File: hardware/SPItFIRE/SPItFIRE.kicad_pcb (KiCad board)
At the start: 2 copper layers, 182.9 x 151.8 mm, 36 parts, among them J1 Compact Host, J10 ISP, J11 Joystick A, J12 Joystick B, J13 Peripheral DE-9, J14 Peripheral User Port, J2 User Port Host, J3 User Port Passthrough, J4 SD Card Adapter, J5 DeadOnRTC, J6 SPI_4, J7 SPI_5, J8 SPI_6, J9 SPI_7, U1 74HC138, U2 ATmega1284P-A, Y1 Crystal

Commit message: Work in progress on layout and routing
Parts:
- moved J1 0.20 mm to (59.4, 66.2)
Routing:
- net ~{SS_5}: track 0.00 -> 111.7 mm, vias 0 -> 2
- net PD1: track 109.8 -> 10.3 mm, vias 3 -> 1
- net ~{SS_3}: track 0.00 -> 85.3 mm, vias 0 -> 2
- net GND: track 128.6 -> 212.5 mm
- net AVCC: track 98.7 -> 24.8 mm, vias 2 -> 0
- net ~{SS_4}: track 20.3 -> 89.2 mm, vias 1 -> 2
- net PA3: track 81.0 -> 16.7 mm, vias 4 -> 2
- net PA1: track 83.4 -> 19.3 mm, vias 4 -> 2
- net PD5: track 62.4 -> 3.43 mm, vias 2 -> 1
- net PB1: track 80.4 -> 22.8 mm, vias 4 -> 2
- net PB3: track 81.5 -> 25.8 mm, vias 4 -> 2
- net PD0: track 99.5 -> 44.4 mm, vias 2 -> 1
- net PC7: track 63.7 -> 11.0 mm, vias 4 -> 2
- net ~{SS_1}: track 3.88 -> 55.4 mm, vias 0 -> 4
- net PA7: track 60.6 -> 10.1 mm, vias 4 -> 2
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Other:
- board size 182.9 x 151.8 mm -> 153 x 151.8 mm

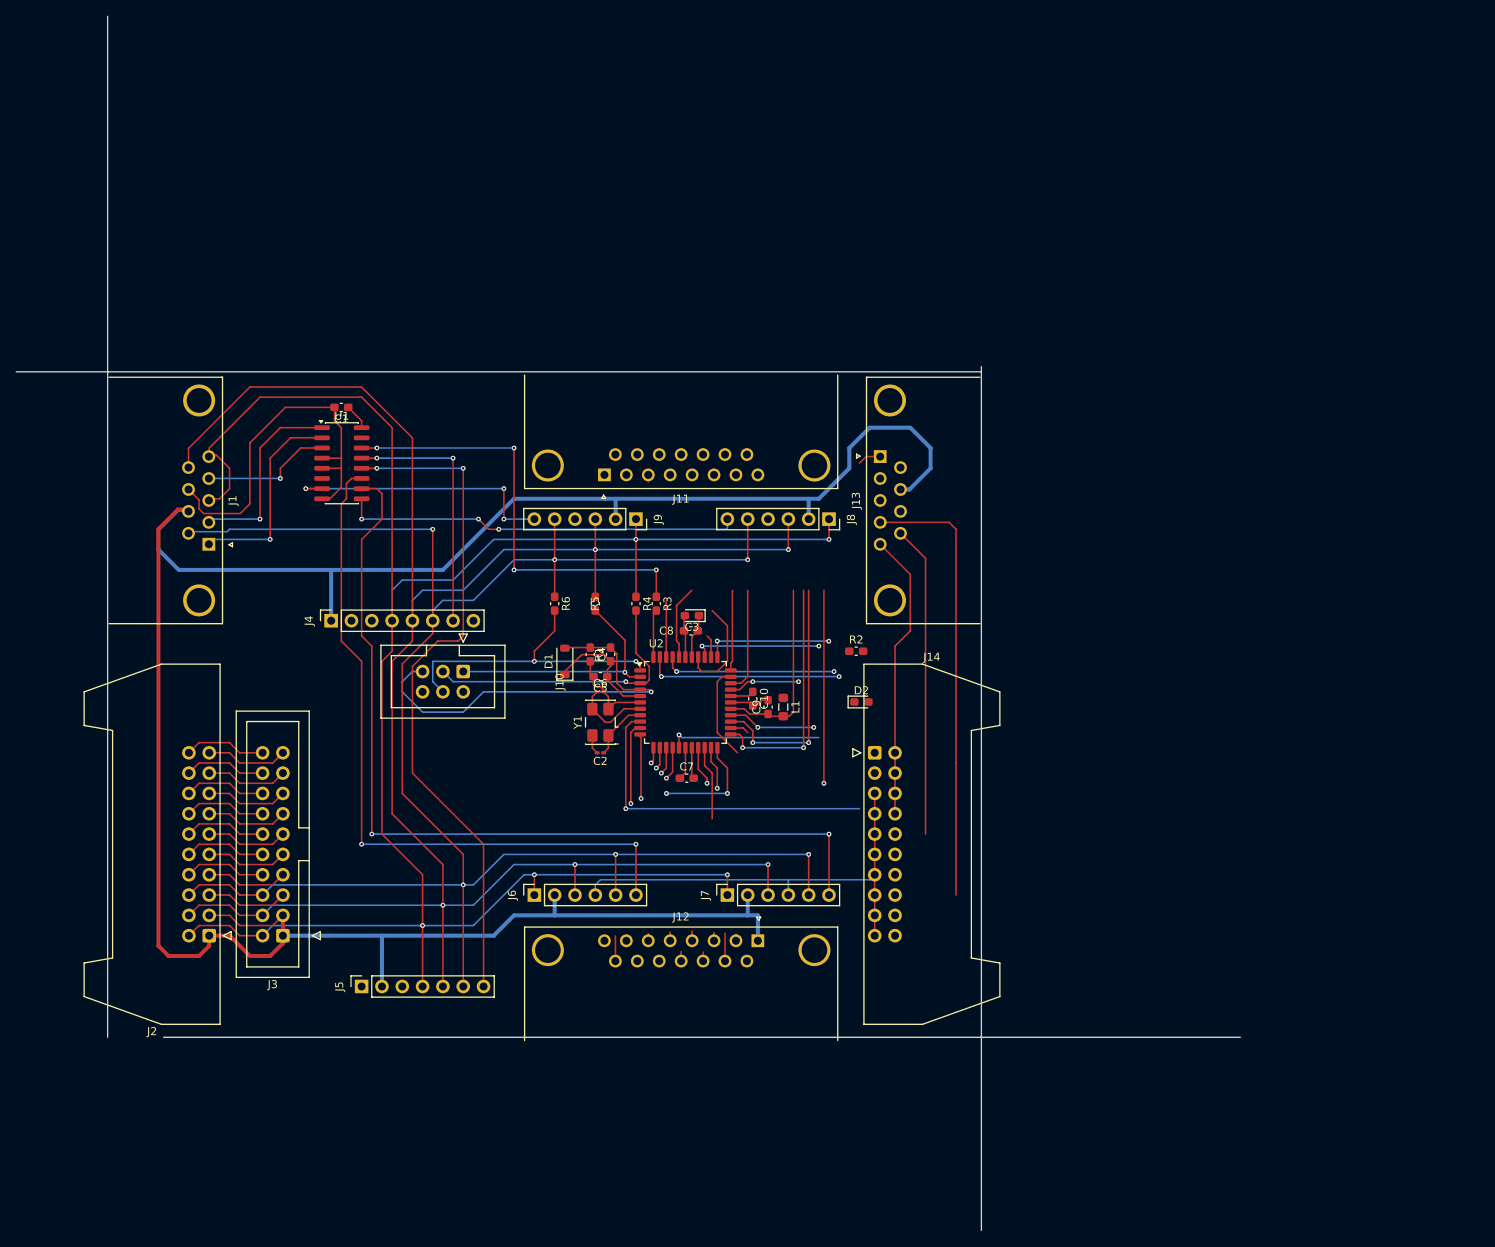
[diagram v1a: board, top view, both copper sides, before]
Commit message: Completed layout and routing. Now need to work through the few DRC errors
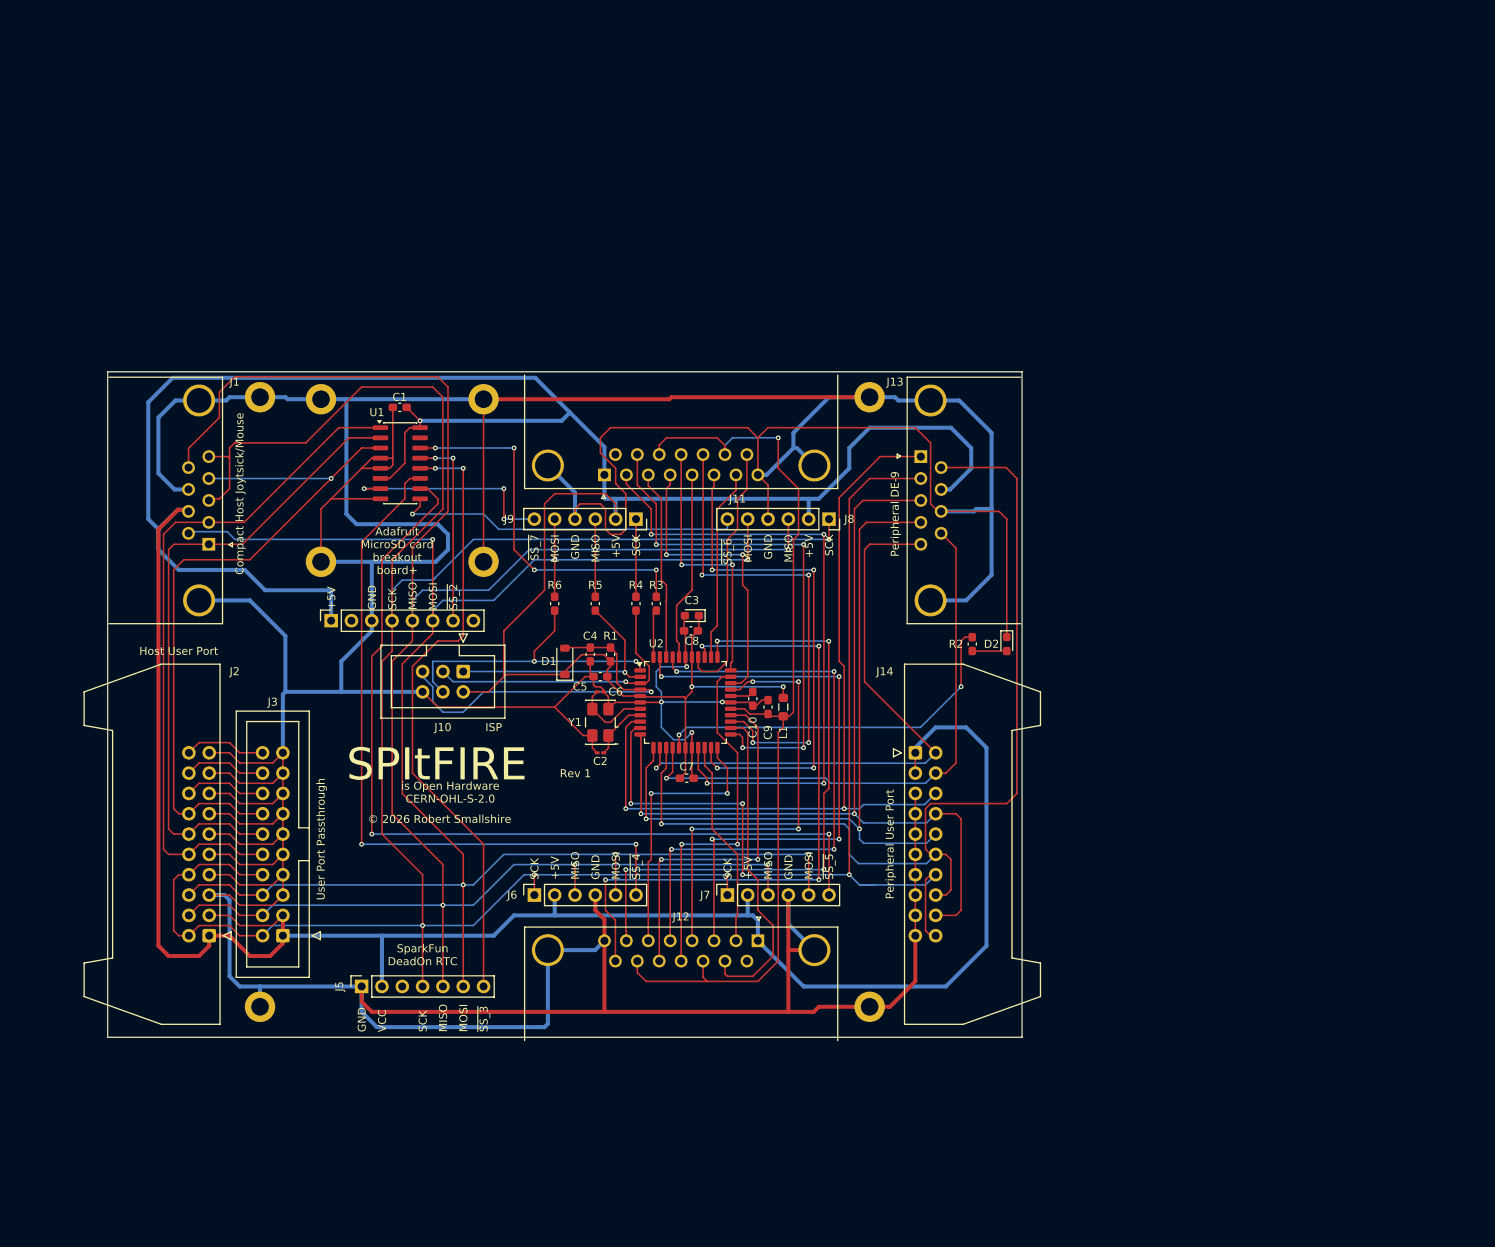
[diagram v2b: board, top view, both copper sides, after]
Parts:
- added H301: MountingHole_Pad, MountingHole:MountingHole_2.2mm_M2_DIN965_Pad, F.Cu at (78.7, 129.5)
- added H302: MountingHole_Pad, MountingHole:MountingHole_2.2mm_M2_DIN965_Pad, F.Cu at (154.9, 129.5)
- added H303: MountingHole_Pad, MountingHole:MountingHole_2.2mm_M2_DIN965_Pad, F.Cu at (154.9, 53.3)
- added H304: MountingHole_Pad, MountingHole:MountingHole_2.2mm_M2_DIN965_Pad, F.Cu at (78.7, 53.3)
- added H305: MountingHole_Pad, MountingHole:MountingHole_2.2mm_M2_DIN965_Pad, F.Cu at (86.4, 73.9)
- added H306: MountingHole_Pad, MountingHole:MountingHole_2.2mm_M2_DIN965_Pad, F.Cu at (106.7, 73.9)
- added H307: MountingHole_Pad, MountingHole:MountingHole_2.2mm_M2_DIN965_Pad, F.Cu at (106.7, 53.6)
- added H308: MountingHole_Pad, MountingHole:MountingHole_2.2mm_M2_DIN965_Pad, F.Cu at (86.4, 53.6)
- J1: value Compact Host -> Compact Host Joytsick/Mouse
- J2: value User Port Host -> Host User Port
- moved D2 19.6 mm to (172.1, 84.2), turned to -90 degrees
- moved R2 14.5 mm to (167.8, 84.2), turned to -90 degrees
- moved C1 7.30 mm to (96.2, 54.6)
- moved U1 7.30 mm to (96.3, 61.6)
- moved J13 5.08 mm to (174.3, 66.2)
- moved J14 5.08 mm to (160.7, 97.8)
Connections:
- J1 pad SH: (no net) -> GND
- J11 pad SH: (no net) -> GND
- J12 pad SH: (no net) -> GND
- J13 pad SH: (no net) -> GND
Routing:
- net GND: track 212.5 -> 861.4 mm, vias 0 -> 4
- net +5V: track 327.0 -> 557.2 mm, vias 0 -> 3
- net PD5: track 3.43 -> 124.8 mm
- net PD1: track 10.3 -> 126.6 mm, vias 1 -> 4
- net PD2: track 8.06 -> 112.9 mm, vias 1 -> 2
- net AVCC: track 24.8 -> 117.7 mm, vias 0 -> 1
- net PA1: track 19.3 -> 82.7 mm, vias 2 -> 4
- net /main/A2: track 26.8 -> 90.0 mm
- net PA3: track 16.7 -> 78.5 mm, vias 2 -> 4
- net PC2: track 5.40 -> 64.4 mm, vias 1 -> 4
- net PD0: track 44.4 -> 103.3 mm, vias 1 -> 2
- net PB1: track 22.8 -> 75.7 mm, vias 2 -> 4
- net /main/A0: track 34.4 -> 86.0 mm, vias 1 -> 0
- net PC0: track 29.7 -> 80.9 mm, vias 2 -> 4
- net PB3: track 25.8 -> 73.7 mm, vias 2 -> 4
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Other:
- board size 153 x 151.8 mm -> 114.3 x 83.2 mm
- board text added: "+5V"
- board text added: "Adafruit MicroSD card breakout board+"
- board text added: "GND"
- board text added: "MISO"
- board text added: "MOSI"
- board text added: "Rev 1"
- board text added: "SCK"
- board text added: "SPItFIRE"
- board text added: "SparkFun DeadOn RTC"
- board text added: "VCC"
- board text added: "is Open Hardware CERN-OHL-S-2.0"
- board text added: "~{SS_2}"
- board text added: "~{SS_3}"
- board text added: "~{SS_4}"
- board text added: "~{SS_5}"
- board text added: "~{SS_6}"
- board text added: "~{SS_7}"
- board text added: "© 2026 Robert Smallshire"

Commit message: Completed layout and passes DRC check
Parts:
- J14, J2: footprint Connector_IDC:IDC-Header_2x10_P2.54mm_Latch_Horizontal -> SPItFIRE:IDC-Header_2x10_P2.54mm_Latch_Horizontal
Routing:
- net PD1: track 126.6 -> 124.7 mm
- net GND: track 861.4 -> 860.7 mm
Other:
- board size 114.3 x 83.2 mm -> 114.3 x 83.8 mm
- board text added: "Joystick Port A"
- board text added: "Joystick Port B"
- board text added: "⌀M2"

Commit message: Replaced footprint for small crystal ballast capacitors
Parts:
- C2, C6: footprint Capacitor_SMD:C_0201_0603Metric_Pad0.64x0.40mm_HandSolder -> Capacitor_SMD:C_0201_0603Metric
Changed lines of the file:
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@@
 		)
 	)
-	(footprint "Capacitor_SMD:C_0201_0603Metric_Pad0.64x0.40mm_HandSolder"
+	(footprint "Capacitor_SMD:C_0201_0603Metric"
 		(layer "F.Cu")
 		(at 121.285 90.17)
-		(descr "Capacitor SMD 0201 (0603 Metric), square (rectangular) end terminal, IPC-7351 nominal with elongated pad for handsoldering. (Body size source: https://www.vishay.com/docs/20052/crcw0201e3.pdf)")
-		(tags "capacitor handsolder")
+		(descr "Capacitor SMD 0201 (0603 Metric), square (rectangular) end terminal, IPC-7351 nominal, (Body size source: https://www.vishay.com/docs/20052/crcw0201e3.pdf)")
+		(tags "capacitor")
 		(property "Reference" "C6"
 			(at 1.905 0 0)
@@
 			)
 		)
-		(property "Description" "Unpolarized capacitor, small symbol"
+		(property "Description" ""
 			(at 0 0 0)
 			(layer "F.Fab")
@@
 		(sheetname "/main/")
 		(sheetfile "main.kicad_sch")
-		(units
-			(unit
-				(name "A")
-				(pins "1" "2")
-			)
-		)
 		(attr smd)
 		(duplicate_pad_numbers_are_jumpers no)
 		(fp_rect
-			(start -0.88 -0.35)
-			(end 0.88 0.35)
+			(start -0.7 -0.35)
+			(end 0.7 0.35)
 			(stroke
 				(width 0.05)
@@
 		)
 		(pad "" smd roundrect
-			(at -0.4325 0)
-			(size 0.458 0.36)
+			(at -0.345 0)
+			(size 0.318 0.36)
 			(layers "F.Paste")
 			(roundrect_rratio 0.25)
 		)
 		(pad "" smd roundrect
-			(at 0.4325 0)
-			(size 0.458 0.36)
+			(at 0.345 0)
+			(size 0.318 0.36)
 			(layers "F.Paste")
 			(roundrect_rratio 0.25)
 		)
 		(pad "1" smd roundrect
-			(at -0.4075 0)
-			(size 0.635 0.4)
+			(at -0.32 0)
+			(size 0.46 0.4)
 			(layers "F.Cu" "F.Mask")
 			(roundrect_rratio 0.25)
@@
 		)
 		(pad "2" smd roundrect
-			(at 0.4075 0)
-			(size 0.635 0.4)
+			(at 0.32 0)
+			(size 0.46 0.4)
 			(layers "F.Cu" "F.Mask")
 			(roundrect_rratio 0.25)
@@
 		)
 	)
-	(footprint "Capacitor_SMD:C_0201_0603Metric_Pad0.64x0.40mm_HandSolder"
+	(footprint "Capacitor_SMD:C_0201_0603Metric"
 		(layer "F.Cu")
 		(at 121.285 97.79 180)
-		(descr "Capacitor SMD 0201 (0603 Metric), square (rectangular) end terminal, IPC-7351 nominal with elongated pad for handsoldering. (Body size source: https://www.vishay.com/docs/20052/crcw0201e3.pdf)")
-		(tags "capacitor handsolder")
+		(descr "Capacitor SMD 0201 (0603 Metric), square (rectangular) end terminal, IPC-7351 nominal, (Body size source: https://www.vishay.com/docs/20052/crcw0201e3.pdf)")
+		(tags "capacitor")
 		(property "Reference" "C2"
-			(at 0 -1.05 0)
+			(at 0 -1.05 180)
 			(layer "F.SilkS")
 			(effects
@@
 		)
 		(property "Value" "C_Small"
-			(at 0 1.05 0)
+			(at 0 1.05 180)
 			(layer "F.Fab")
 			(effects
@@
 		)
 		(property "Datasheet" ""
-			(at 0 0 0)
+			(at 0 0 180)
 			(layer "F.Fab")
 			(hide yes)
@@
 			)
 		)
-		(property "Description" "Unpolarized capacitor, small symbol"
-			(at 0 0 0)
+		(property "Description" ""
+			(at 0 0 180)
 			(layer "F.Fab")
 			(hide yes)
@@
 		)
 		(property "KiLib_Generator" "SMD_2terminal_chip_molded"
-			(at 0 0 0)
+			(at 0 0 180)
 			(layer "F.SilkS")
 			(hide yes)
@@
 		(sheetname "/main/")
 		(sheetfile "main.kicad_sch")
-		(units
-			(unit
-				(name "A")
-				(pins "1" "2")
-			)
-		)
 		(attr smd)
 		(duplicate_pad_numbers_are_jumpers no)
 		(fp_rect
-			(start -0.88 -0.35)
-			(end 0.88 0.35)
+			(start -0.7 -0.35)
+			(end 0.7 0.35)
 			(stroke
 				(width 0.05)
@@
 		)
 		(fp_text user "${REFERENCE}"
-			(at 0 -0.68 0)
+			(at 0 -0.68 180)
 			(layer "F.Fab")
 			(effects
@@
 		)
 		(pad "" smd roundrect
-			(at -0.4325 0 180)
-			(size 0.458 0.36)
+			(at -0.345 0 180)
+			(size 0.318 0.36)
 			(layers "F.Paste")
 			(roundrect_rratio 0.25)
 		)
 		(pad "" smd roundrect
-			(at 0.4325 0 180)
-			(size 0.458 0.36)
+			(at 0.345 0 180)
+			(size 0.318 0.36)
 			(layers "F.Paste")
 			(roundrect_rratio 0.25)
 		)
 		(pad "1" smd roundrect
-			(at -0.4075 0 180)
-			(size 0.635 0.4)
+			(at -0.32 0 180)
+			(size 0.46 0.4)
 			(layers "F.Cu" "F.Mask")
 			(roundrect_rratio 0.25)
@@
 		)
 		(pad "2" smd roundrect
-			(at 0.4075 0 180)
-			(size 0.635 0.4)
+			(at 0.32 0 180)
+			(size 0.46 0.4)
 			(layers "F.Cu" "F.Mask")
 			(roundrect_rratio 0.25)
